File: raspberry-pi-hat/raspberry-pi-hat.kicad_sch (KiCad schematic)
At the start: 1 part, among them P1 RaspberryPi-GPIO-header

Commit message: wip
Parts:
- added D1: IR_IN_LED, symbol Device:LED
- added J1: AudioJack3, symbol Connector_Audio:AudioJack3
- added Q1: PMOS, symbol Simulation_SPICE:PMOS
- added R1, R2: R, symbol Device:R
- added U1: MCP3204, symbol Analog_ADC:MCP3204
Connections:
- net +3.3V: now reaches P1.1 (3v3_Out)
- net +3.3V: now also J1.S, Q1.3 (S), R2.1, U1.13 (Vref), U1.14 (Vdd)
- net IR_IN: now reaches P1.11 (BCM17)
- net IR_IN: now also J1.R, Q1.2 (G), R2.2
- net IR_OUT: now reaches P1.12 (PWM0)
- net GND: now reaches P1.14 (GND)
- net GND: now also P1.20 (GND), P1.25 (GND), P1.30 (GND), P1.34 (GND), P1.39 (GND), P1.6 (GND), P1.9 (GND), D1.1 (K), J1.T, U1.12 (AGND), U1.7 (DGND)
- net MOSI: now reaches P1.19 (MOSI)
- net MOSI: now also U1.9 (Din)
- net +5V: now reaches P1.2 (5v_Out)
- net +5V: now also P1.4 (5v_Out)
- net MISO: now reaches P1.21 (MISO)
- net MISO: now also U1.10 (Dout)
- net SCLK: now reaches P1.23 (SCLK)
- net SCLK: now also U1.11 (CLK)
- net ADC_CS: now reaches P1.24 (CE0)
- net ADC_CS: now also U1.8 (~{CS}/SHDN)
- new net: D1.2 (A), R1.2
- new net: Q1.1 (D), R1.1
- no-connect marks 0 -> 23

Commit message: initial schematic
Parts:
- removed Q1: PMOS, symbol Simulation_SPICE:PMOS
- added C1, C2: C, symbol Device:C
- added D2: IR_OUT_LED, symbol Device:LED
- added J2: IR_OUT_JACK, symbol Connector_Audio:AudioJack3
- added J3, J4: IR_IN_JACK, symbol Connector_Audio:AudioJack3
- added Q1: 2N7002K, Package_TO_SOT_SMD:SOT-23, symbol Transistor_FET:2N7002K
- added R10, R11, R3, R4, R5, R6, R7, R8, R9: R, symbol Device:R
- added U2: 74AC86, symbol 74xx:74LS86
- J1: value AudioJack3 -> IR_IN_JACK
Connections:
- net +3.3V: now also Q1.3 (D), R10.2, R7.2, U2.14 (VCC)
- net +5V: no longer P1.4 (5v_Out)
- net GND: now also U1.3 (CH2), U1.4 (CH3), C1.2, C2.2, D2.1 (K), J2.R, J2.S, R11.1, R6.1, U2.10, U2.12, U2.13, U2.7 (GND)
- net IR_IN: now also R1.1, U2.3; no longer J1.R, R2.2
- net IR_OUT: now also U2.4, U2.9
- net IR_OUT_POL: now reaches P1.16 (BCM23)
- net IR_OUT_POL: now also U2.5
- net IR_IN_POL: now reaches P1.22 (BCM25)
- net IR_IN_POL: now also U2.2
- net ADC_CH0: now reaches U1.1 (CH0)
- net ADC_CH0: now also J3.T, R8.2
- net ADC_CH1: now reaches U1.2 (CH1)
- net ADC_CH1: now also J4.T, R9.2
- new net: C1.1, J3.S, R6.2, R7.1, R8.1
- new net: J1.R, R2.2, U2.1
- new net: R3.1, U2.6
- new net: Q1.1 (G), R3.2
- new net: Q1.2 (S), R4.2
- new net: D2.2 (A), R5.1
- new net: R5.2, U2.8
- new net: C2.1, J4.S, R10.1, R11.2, R9.1
- new net: J2.T, R4.1
- no-connect marks 23 -> 25
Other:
- moved on the sheet: D1, J1, P1, R2, U1

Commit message: wip
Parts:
- added C3: C, symbol Device:C
- added J5: IR_IN_JMP, symbol Connector_Generic:Conn_02x03_Odd_Even
- added J6: IR_OUT_JMP, symbol Connector_Generic:Conn_02x03_Odd_Even
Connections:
- net +3.3V: now also C3.1, J5.2 (Pin_2); no longer J1.S
- net GND: now also C3.2, J5.6 (Pin_6), J6.3 (Pin_3), J6.5 (Pin_5); no longer J1.T, J2.R, J2.S
- net at R2.2, U2.1: now also J5.4 (Pin_4); no longer J1.R
- net at R4.1: now also J6.1 (Pin_1); no longer J2.T
- new net: J1.S, J5.1 (Pin_1)
- new net: J1.R, J5.3 (Pin_3)
- new net: J1.T, J5.5 (Pin_5)
- new net: J2.T, J6.2 (Pin_2)
- new net: J2.R, J6.4 (Pin_4)
- new net: J2.S, J6.6 (Pin_6)
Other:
- moved on the sheet: C1, C2, D1, D2, J1, J2, J3, J4, Q1, R1, R10, R11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

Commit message: rev
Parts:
- added C4, C5: 0.1uF, symbol Device:C
- C1, C2: value C -> 10uF
- C3: value C -> 0.1uF
- J1, J2: symbol Connector_Audio:AudioJack3 -> Connector_Audio:AudioJack4
- J3: value IR_IN_JACK -> ADC0_JACK; symbol Connector_Audio:AudioJack3 -> Connector_Audio:AudioJack4
- J4: value IR_IN_JACK -> ADC1_JACK; symbol Connector_Audio:AudioJack3 -> Connector_Audio:AudioJack4
- P1: value RaspberryPi-GPIO-header -> RPi-GPIO
- Q1: value 2N7002K -> IRLML2803TRPBF
- R1, R4, R5: value R -> 180R
- R10, R11, R2, R6, R7: value R -> 10K
- R3: value R -> 100R
- R8, R9: value R -> 33R
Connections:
- net +3.3V: now also R4.2, R5.2, C4.1, C5.1; no longer Q1.3 (D)
- net IR_OUT: no longer U2.9
- net at Q1.2 (S): no longer R4.2
- net at J1.S, J5.1 (Pin_1): now also J1.R2
- net at J5.3 (Pin_3): now also J1.R1; no longer J1.R
- net at J6.4 (Pin_4): now also J2.R1; no longer J2.R
- net at J2.S, J6.6 (Pin_6): now also J2.R2
- net at U2.8: no longer R5.2
- removed net GND: C1.2, C2.2, C3.2, D1.1 (K), D2.1 (K), J5.6 (Pin_6), J6.3 (Pin_3), J6.5 (Pin_5), P1.14 (GND), P1.20 (GND), P1.25 (GND), P1.30 (GND), P1.34 (GND), P1.39 (GND), P1.6 (GND), P1.9 (GND), R11.1, R6.1, U1.12 (AGND), U1.3 (CH2), U1.4 (CH3), U1.7 (DGND), U2.10, U2.12, U2.13, U2.7 (GND)
- new net: P1.14 (GND), P1.20 (GND), P1.30 (GND), P1.34 (GND), P1.6 (GND)
- new net: P1.25 (GND), P1.39 (GND), P1.9 (GND)
- new net: D2.1 (K), J6.3 (Pin_3), J6.5 (Pin_5), Q1.3 (D)
- new net: U2.12, U2.13
- new net: U2.10, U2.9
- new net: U1.12 (AGND), U1.7 (DGND)
- new net: U1.3 (CH2), U1.4 (CH3)
- no-connect marks 25 -> 28
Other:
- moved on the sheet: C1, C2, D2, J6, Q1, R10, R11, R3, R4, R5, R6, R7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

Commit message: pcb
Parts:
- C1, C2, C3, C4, C5: footprint (none) -> Capacitor_SMD:C_0805_2012Metric_Pad1.18x1.45mm_HandSolder
- D1, D2: footprint (none) -> LED_SMD:LED_0805_2012Metric_Pad1.15x1.40mm_HandSolder
- J1, J2, J3, J4: footprint (none) -> raspberry-pi-hat:54-00174_TEN
- J5, J6: footprint (none) -> Connector_PinHeader_2.54mm:PinHeader_2x03_P2.54mm_Vertical
- P1: footprint Pin_Headers:Pin_Header_Straight_2x20 -> Connector_PinHeader_2.54mm:PinHeader_2x20_P2.54mm_Vertical
- R1, R10, R11, R2, R3, R4, R5, R6, R7, R8, R9: footprint (none) -> Resistor_SMD:R_0805_2012Metric_Pad1.20x1.40mm_HandSolder
- U1, U2: footprint (none) -> Package_SO:SOIC-14_3.9x8.7mm_P1.27mm
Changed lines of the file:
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@@
 			)
 		)
-		(property "Footprint" "Pin_Headers:Pin_Header_Straight_2x20"
+		(property "Footprint" "Connector_PinHeader_2.54mm:PinHeader_2x20_P2.54mm_Vertical"
 			(at 49.53 88.9 0)
 			(effects
@@
 			)
 		)
-		(property "Footprint" ""
+		(property "Footprint" "LED_SMD:LED_0805_2012Metric_Pad1.15x1.40mm_HandSolder"
 			(at 264.16 137.16 0)
 			(effects
@@
 			)
 		)
-		(property "Footprint" ""
+		(property "Footprint" "Resistor_SMD:R_0805_2012Metric_Pad1.20x1.40mm_HandSolder"
 			(at 123.19 177.292 90)
 			(effects
@@
 			)
 		)
-		(property "Footprint" ""
+		(property "Footprint" "Resistor_SMD:R_0805_2012Metric_Pad1.20x1.40mm_HandSolder"
 			(at 235.712 107.95 90)
 			(effects
@@
 			)
 		)
-		(property "Footprint" ""
+		(property "Footprint" "Capacitor_SMD:C_0805_2012Metric_Pad1.18x1.45mm_HandSolder"
 			(at 77.1652 176.53 0)
 			(effects
@@
 			)
 		)
-		(property "Footprint" ""
+		(property "Footprint" "Package_SO:SOIC-14_3.9x8.7mm_P1.27mm"
 			(at 252.73 116.84 0)
 			(effects
@@
 			)
 		)
-		(property "Footprint" ""
+		(property "Footprint" "Resistor_SMD:R_0805_2012Metric_Pad1.20x1.40mm_HandSolder"
 			(at 207.01 58.928 90)
 			(effects
@@
 			)
 		)
-		(property "Footprint" ""
+		(property "Footprint" "raspberry-pi-hat:54-00174_TEN"
 			(at 102.87 173.99 0)
 			(effects
@@
 			)
 		)
-		(property "Footprint" ""
+		(property "Footprint" "Connector_PinHeader_2.54mm:PinHeader_2x03_P2.54mm_Vertical"
 			(at 215.9 114.3 0)
 			(effects
@@
 			)
 		)
-		(property "Footprint" ""
+		(property "Footprint" "raspberry-pi-hat:54-00174_TEN"
 			(at 201.93 111.76 0)
 			(effects
@@
 			)
 		)
-		(property "Footprint" ""
+		(property "Footprint" "Package_SO:SOIC-14_3.9x8.7mm_P1.27mm"
 			(at 96.52 86.36 0)
 			(effects
@@
 			)
 		)
-		(property "Footprint" ""
+		(property "Footprint" "Connector_PinHeader_2.54mm:PinHeader_2x03_P2.54mm_Vertical"
 			(at 243.84 43.18 0)
 			(effects
@@
 			)
 		)
-		(property "Footprint" ""
+		(property "Footprint" "Resistor_SMD:R_0805_2012Metric_Pad1.20x1.40mm_HandSolder"
 			(at 218.948 31.75 90)
 			(effects
@@
 			)
 		)
-		(property "Footprint" ""
+		(property "Footprint" "raspberry-pi-hat:54-00174_TEN"
 			(at 170.18 173.99 0)
 			(effects
@@
 			)
 		)
-		(property "Footprint" ""
+		(property "Footprint" "Resistor_SMD:R_0805_2012Metric_Pad1.20x1.40mm_HandSolder"
 			(at 203.708 163.83 90)
 			(effects
@@
 			)
 		)
-		(property "Footprint" ""
+		(property "Footprint" "Resistor_SMD:R_0805_2012Metric_Pad1.20x1.40mm_HandSolder"
 			(at 136.398 163.83 90)
 			(effects
@@
 			)
 		)
-		(property "Footprint" ""
+		(property "Footprint" "Resistor_SMD:R_0805_2012Metric_Pad1.20x1.40mm_HandSolder"
 			(at 136.398 179.07 90)
 			(effects
@@
 			)
 		)
-		(property "Footprint" ""
+		(property "Footprint" "Resistor_SMD:R_0805_2012Metric_Pad1.20x1.40mm_HandSolder"
 			(at 203.708 179.07 90)
 			(effects
@@
 			)
 		)
-		(property "Footprint" ""
+		(property "Footprint" "Resistor_SMD:R_0805_2012Metric_Pad1.20x1.40mm_HandSolder"
 			(at 262.382 127 90)
 			(effects
@@
 			)
 		)
-		(property "Footprint" ""
+		(property "Footprint" "Capacitor_SMD:C_0805_2012Metric_Pad1.18x1.45mm_HandSolder"
 			(at 145.7452 182.88 0)
 			(effects
@@
 			)
 		)
-		(property "Footprint" ""
+		(property "Footprint" "raspberry-pi-hat:54-00174_TEN"
 			(at 260.35 45.72 0)
 			(effects
@@
 			)
 		)
-		(property "Footprint" ""
+		(property "Footprint" "Package_SO:SOIC-14_3.9x8.7mm_P1.27mm"
 			(at 123.19 86.36 0)
 			(effects
@@
 			)
 		)
-		(property "Footprint" ""
+		(property "Footprint" "Package_SO:SOIC-14_3.9x8.7mm_P1.27mm"
 			(at 64.77 179.07 0)
 			(effects
@@
 			)
 		)
-		(property "Footprint" ""
+		(property "Footprint" "Resistor_SMD:R_0805_2012Metric_Pad1.20x1.40mm_HandSolder"
 			(at 190.5 177.292 90)
 			(effects
@@
 			)
 		)
-		(property "Footprint" ""
+		(property "Footprint" "Capacitor_SMD:C_0805_2012Metric_Pad1.18x1.45mm_HandSolder"
 			(at 213.0552 182.88 0)
 			(effects
@@
 			)
 		)
-		(property "Footprint" ""
+		(property "Footprint" "Resistor_SMD:R_0805_2012Metric_Pad1.20x1.40mm_HandSolder"
 			(at 235.458 31.75 90)
 			(effects
@@
 			)
 		)
-		(property "Footprint" ""
+		(property "Footprint" "Package_SO:SOIC-14_3.9x8.7mm_P1.27mm"
 			(at 93.98 45.72 0)
 			(effects
@@
 			)
 		)
-		(property "Footprint" ""
+		(property "Footprint" "LED_SMD:LED_0805_2012Metric_Pad1.15x1.40mm_HandSolder"
 			(at 217.17 41.91 0)
 			(effects
@@
 			)
 		)
-		(property "Footprint" ""
+		(property "Footprint" "Capacitor_SMD:C_0805_2012Metric_Pad1.18x1.45mm_HandSolder"
 			(at 115.2652 50.8 0)
 			(effects
@@
 			)
 		)
-		(property "Footprint" ""
+		(property "Footprint" "Package_SO:SOIC-14_3.9x8.7mm_P1.27mm"
 			(at 193.04 57.15 0)
 			(effects
@@
 			)
 		)
-		(property "Footprint" ""
+		(property "Footprint" "Capacitor_SMD:C_0805_2012Metric_Pad1.18x1.45mm_HandSolder"
 			(at 185.1152 118.11 0)
 			(effects

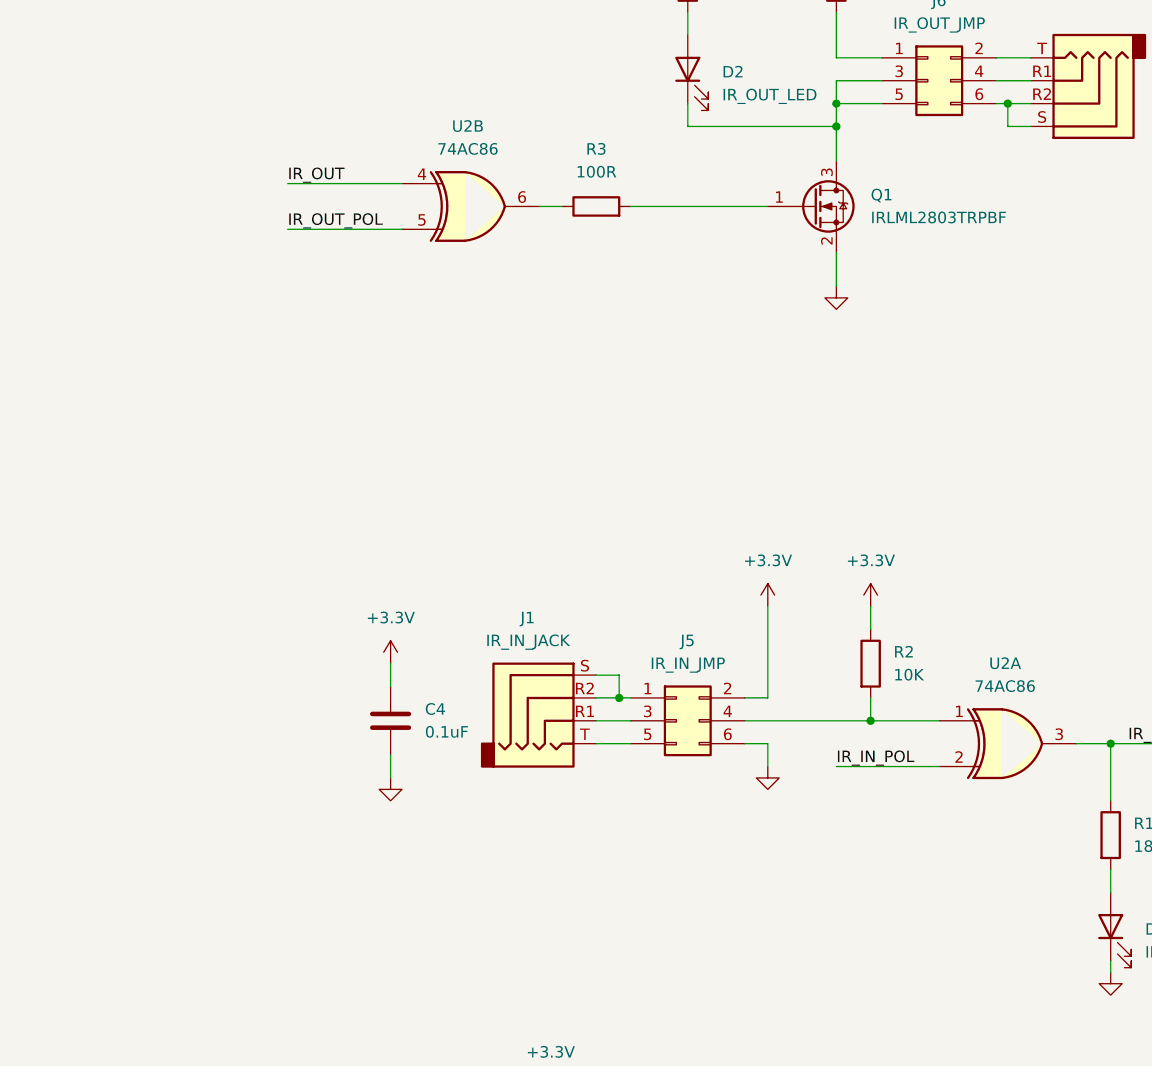
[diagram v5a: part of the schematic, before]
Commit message: add initial state resistors
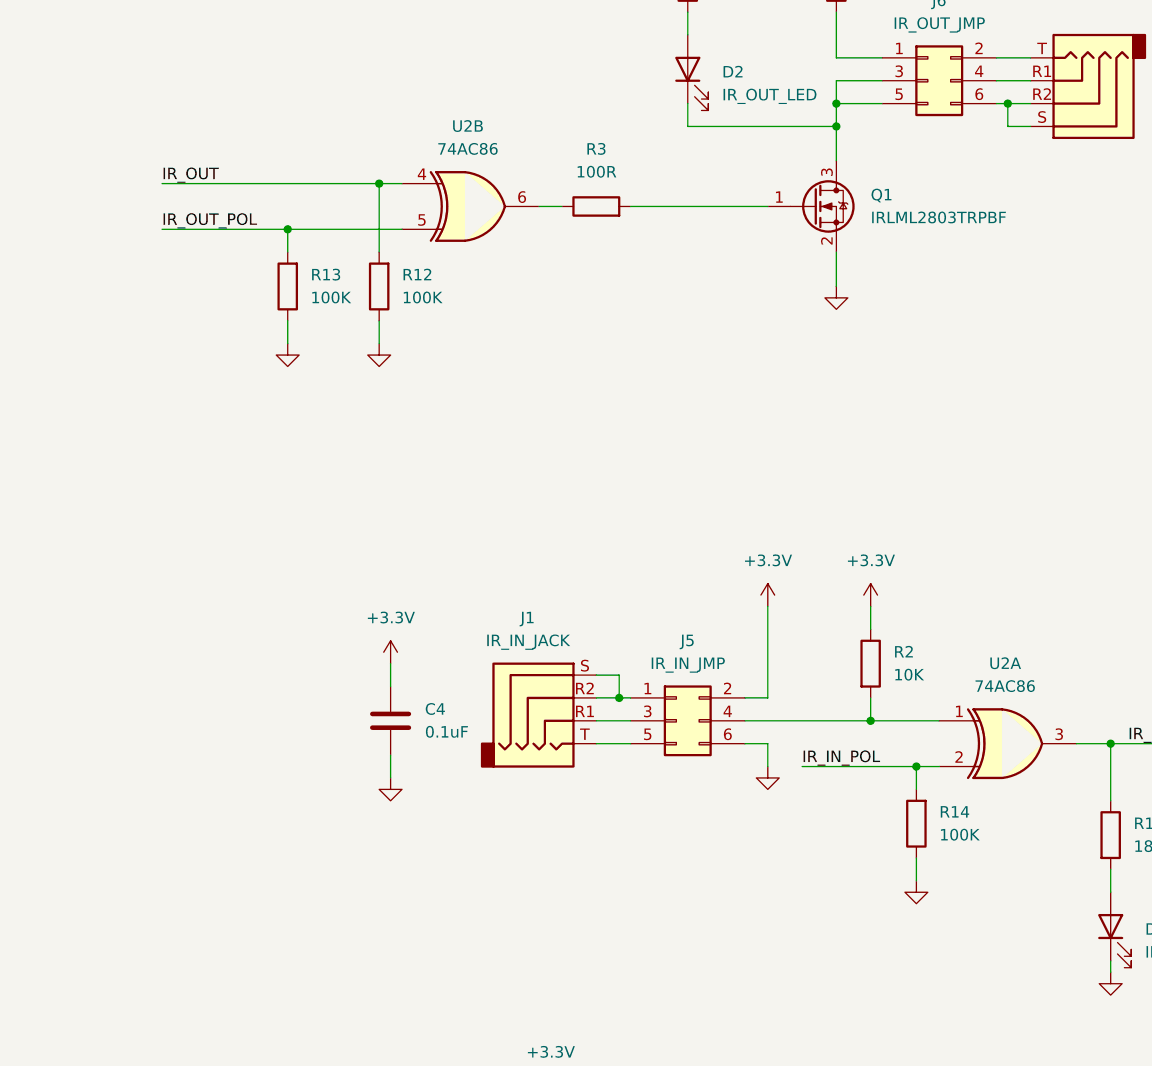
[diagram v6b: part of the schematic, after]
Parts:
- added R12, R13, R14: 100K, Resistor_SMD:R_0805_2012Metric_Pad1.20x1.40mm_HandSolder, symbol Device:R
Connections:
- net IR_IN_POL: now also R14.2
- net IR_OUT: now also R12.2
- net IR_OUT_POL: now also R13.2

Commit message: initial pcb
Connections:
- net GND: now reaches P1.14 (GND), P1.20 (GND), P1.30 (GND), P1.34 (GND), P1.6 (GND)
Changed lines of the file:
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@@
 			)
 		)
-		(property "Value" "~"
+		(property "Value" "GND"
 			(at 66.04 83.82 0)
 			(effects

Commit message: pcb layout
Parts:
- removed C4: 0.1uF, Capacitor_SMD:C_0805_2012Metric_Pad1.18x1.45mm_HandSolder, symbol Device:C
- added C6, C7: 100uF, Capacitor_SMD:CP_Elec_5x5.3, symbol Device:C_Polarized
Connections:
- net GND: now also C1.2, C2.2, C3.2, C5.2, D1.1 (K), J5.6 (Pin_6), P1.25 (GND), P1.39 (GND), P1.9 (GND), Q1.2 (S), R11.1, R12.1, R13.1, R14.1, R6.1, U1.12 (AGND), U1.3 (CH2), U1.4 (CH3), U1.7 (DGND), U2.10, U2.12, U2.13, U2.7 (GND), U2.9, C6.2, C7.2
- net at C1.1, J3.S, R6.2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: now also C6.1
- net at D2.1 (K), J6.5 (Pin_5), Q1.3 (D): no longer J6.3 (Pin_3)
- net at J1.R2, J1.S: now also J5.5 (Pin_5); no longer J5.1 (Pin_1)
- net at J1.T: now also J5.1 (Pin_1); no longer J5.5 (Pin_5)
- net at C2.1, J4.S, R10.1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: now also C7.1
- no-connect marks 28 -> 29
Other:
- moved on the sheet: C2, J1, J4, R10, R11, R9
